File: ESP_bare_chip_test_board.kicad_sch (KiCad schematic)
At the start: 5 parts

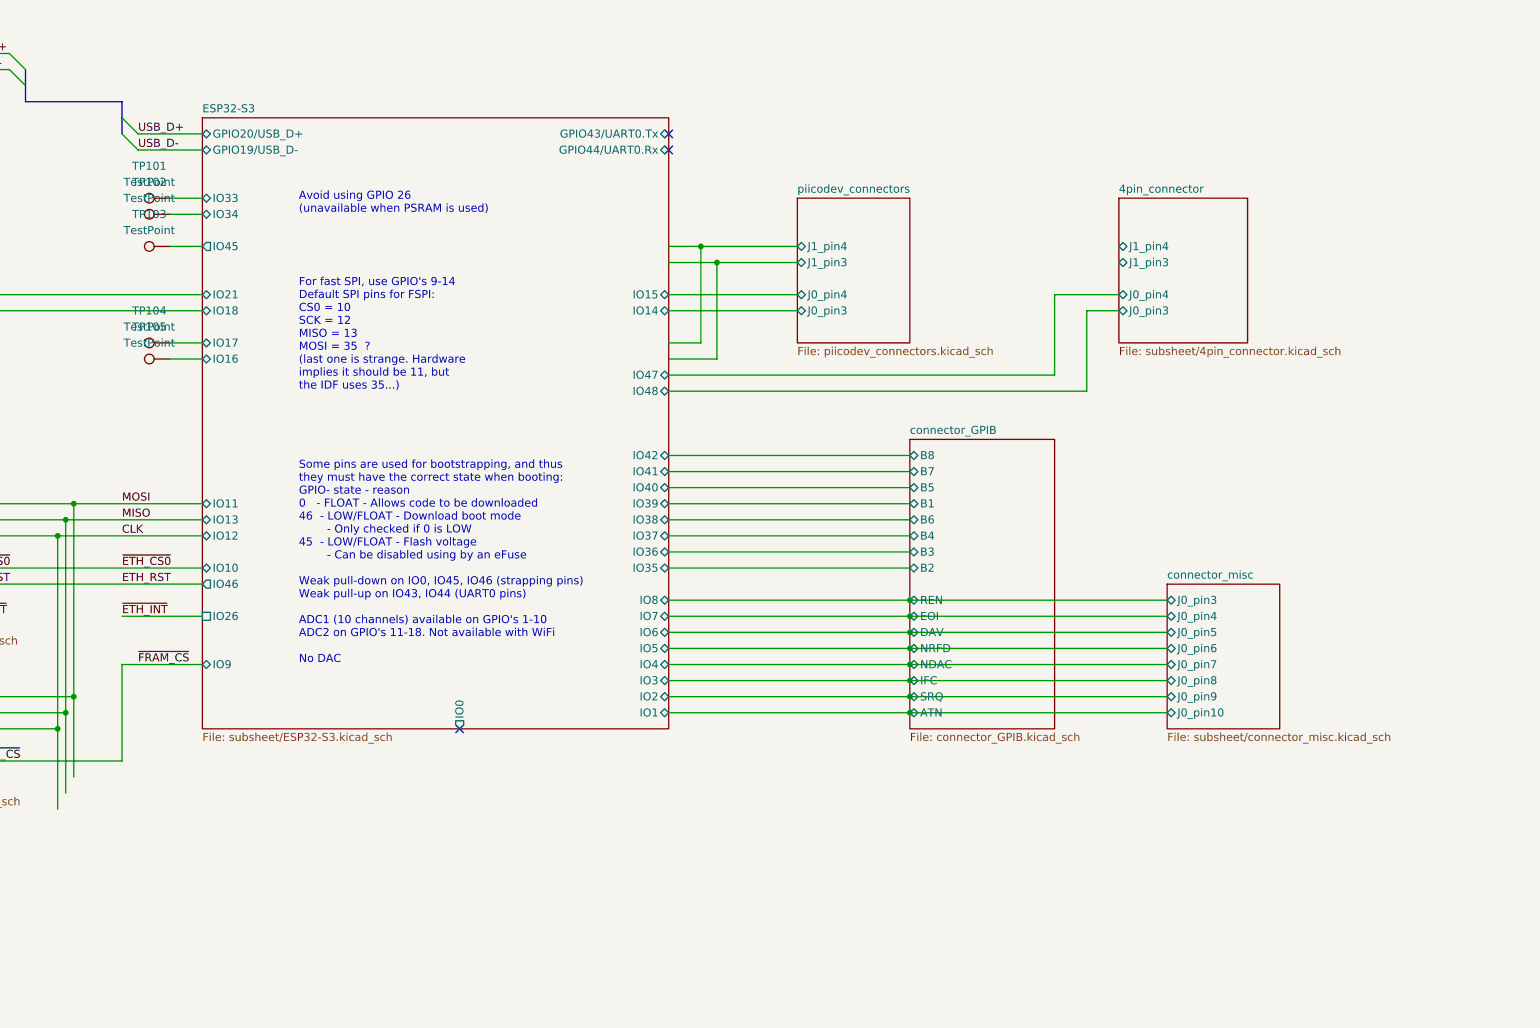
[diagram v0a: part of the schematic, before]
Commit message: Free up IO26 (to allow for PSRAM)
Had spare IO lines, so may as well use a different one to do ETH_INT
instead of IO26.
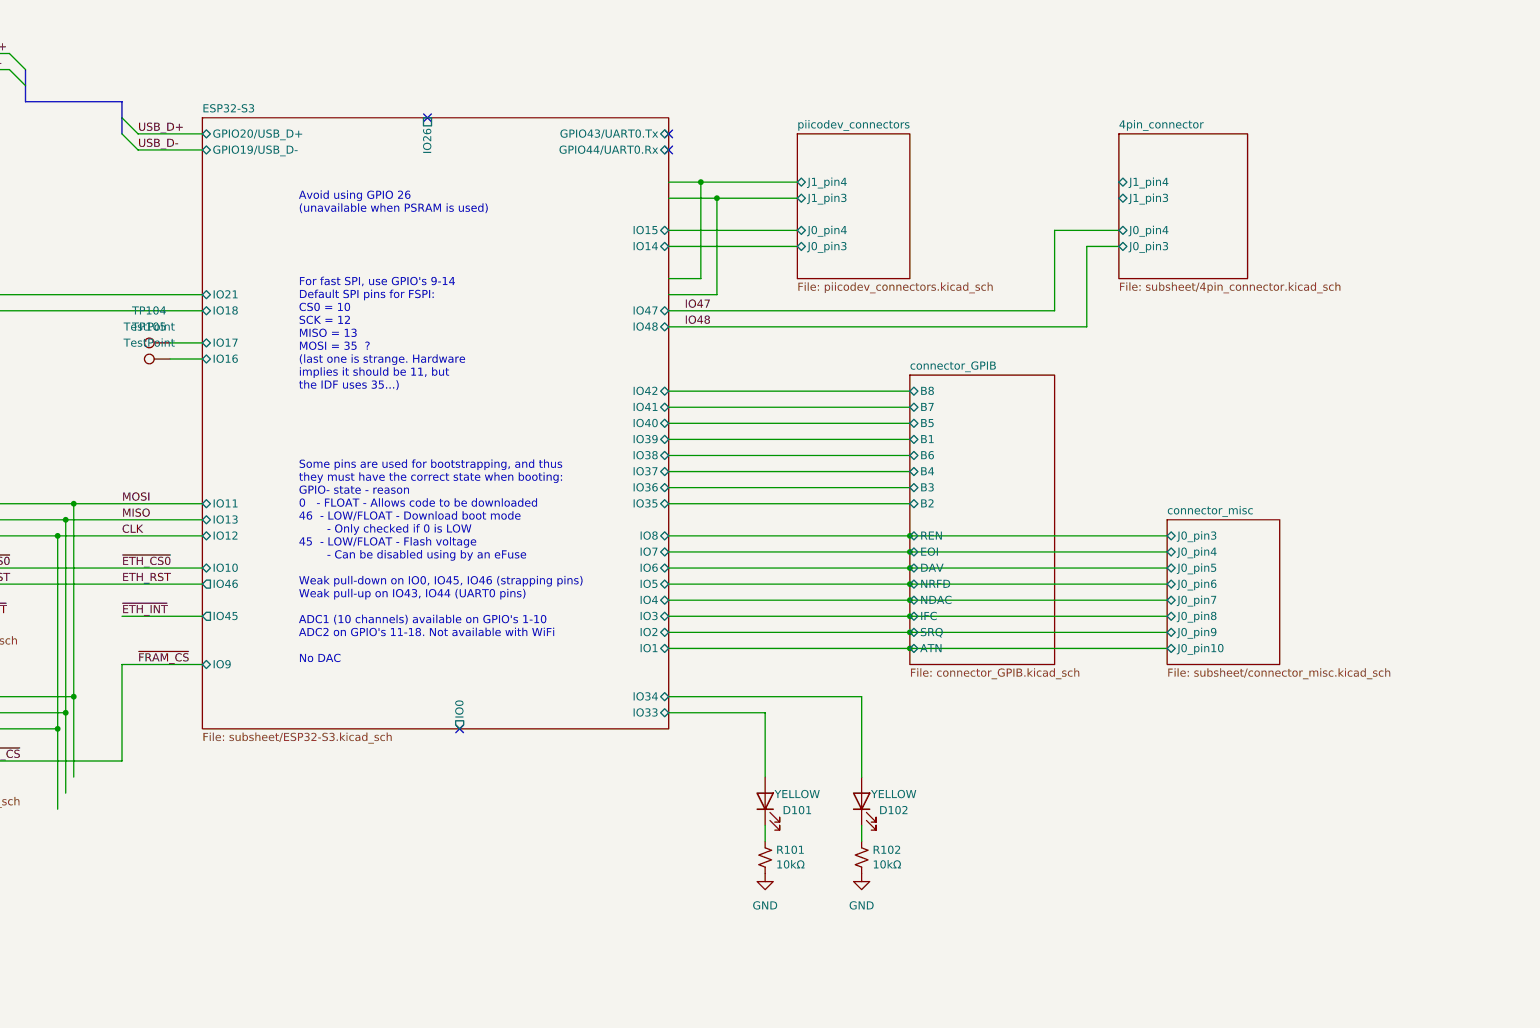
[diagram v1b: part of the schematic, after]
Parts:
- removed TP101, TP102, TP103: TestPoint, TestPoint:TestPoint_Pad_D2.0mm, symbol Connector:TestPoint
- added D101, D102: YELLOW, LED_SMD:LED_0603_1608Metric, symbol Device:LED
- added R101, R102: 10kΩ, Resistor_SMD:R_0603_1608Metric, symbol Device:R_Small_US
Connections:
- net ESP32-S3/IO33: now also D101.2 (A)
- net ESP32-S3/IO34: now also D102.2 (A)
- new net: D101.1 (K), R101.1
- new net: D102.1 (K), R102.1
- new net GND: R101.2, R102.2
- no-connect marks 3 -> 4

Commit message: Silkscreen work. Edit tittle block/version number
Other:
- company: (c) -> (c) Vincent Dalstra
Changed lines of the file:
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@@
 	(title_block
 		(title "Untitled 4-layer JLCPCB")
-		(date "1984/04/01")
-		(rev "v1.0.0")
-		(company "(c)")
-		(comment 1 "Drawn by:")
+		(date "2024-06-14")
+		(rev "1.0.0")
+		(company "(c) Vincent Dalstra")
+		(comment 1 "Drawn by: VGD")
 		(comment 2 "Check by:")
 	)

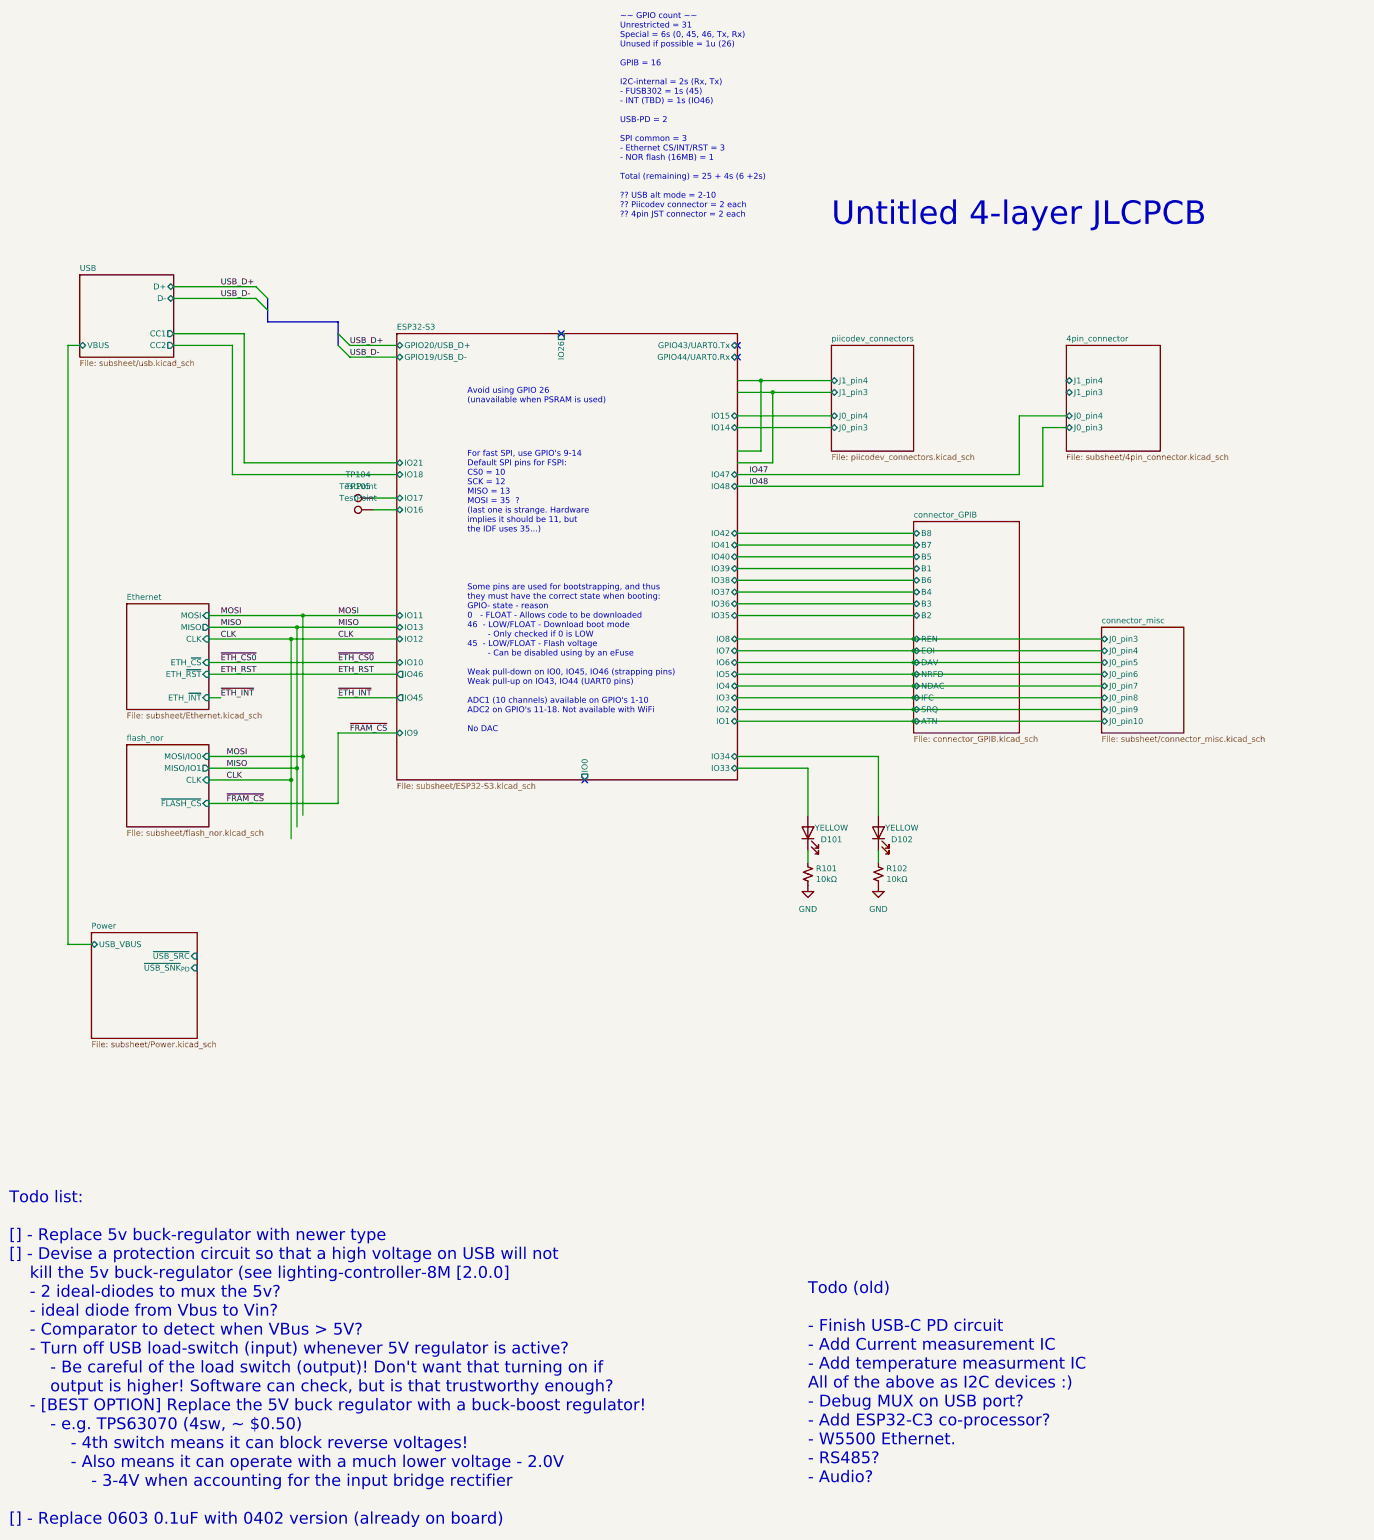
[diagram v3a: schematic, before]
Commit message: Move all subsheets into 'main' subsheet, below root
Keeping all the subsheets in a dedicated 'subsheet' folder makes things
much, much neater. However, specifying filepaths for subsheets has an
interesting problem; they use paths RELATIVE TO THE PARENT SHEET.

The consequence of is that if a subsheet is part of the root sheet, it
needs to be prefixed with 'subsheet/', but NOT if it's further down.
This inconsistency can be resolved by having a single 'main' sheet at
the top that doesn't move.

It's also useful to have a top-level space to put down changelogs,
descriptions etc.
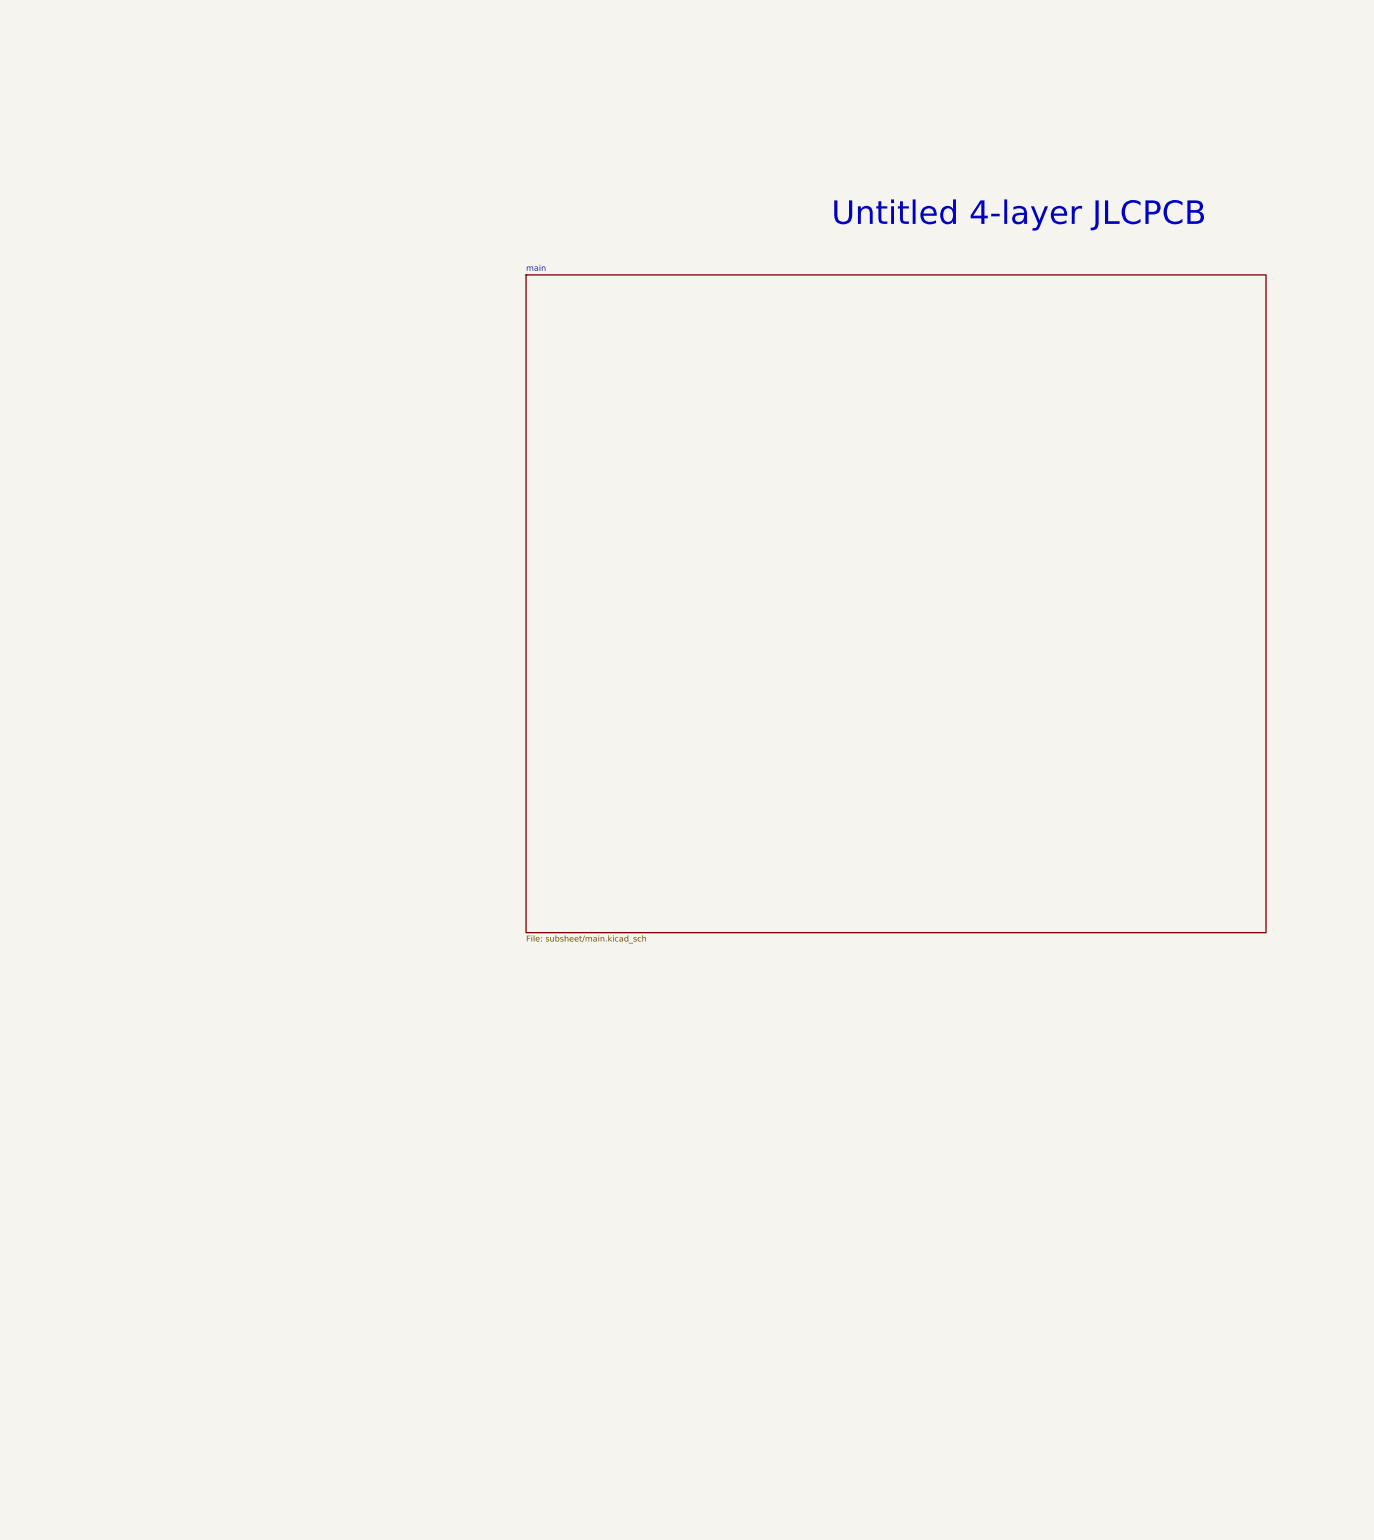
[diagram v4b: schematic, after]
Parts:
- removed D101, D102: YELLOW, LED_SMD:LED_0603_1608Metric, symbol Device:LED
- removed R101, R102: 10kΩ, Resistor_SMD:R_0603_1608Metric, symbol Device:R_Small_US
- removed TP104, TP105: TestPoint, TestPoint:TestPoint_Pad_D2.0mm, symbol Connector:TestPoint
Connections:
- no-connect marks 4 -> 0
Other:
- removed sheet 4pin_connector
- removed sheet ESP32-S3
- removed sheet Ethernet
- removed sheet Power
- removed sheet USB
- removed sheet connector_GPIB
- removed sheet connector_misc
- removed sheet flash_nor
- removed sheet piicodev_connectors
- added sheet main (subsheet/main.kicad_sch)
- note removed: "Avoid using GPIO 26 (unavailable when PSRAM is used)"
- note removed: "For fast SPI, use GPIO's 9-14 Default SPI pins for FSPI: CS0 = 10 SCK = 12 MISO = 13 MOSI = 35 ? (last one is strange. Hardware implies it should be 11, but the IDF uses 35...)"
- note removed: "Some pins are used for bootstrapping, and thus they must have the correct state when booting: GPIO- state - reason 0 - FLOAT - Allows code to be downloaded 46 - LOW/FLOAT - Download boot mode - Only checked if 0 is LOW 45 - LOW/FLOAT - Flash voltage - Can be disabled using by an eFuse Weak pull-down on IO0, IO45, IO46 (strapping pins) Weak pull-up on IO43, IO44 (UART0 pins) ADC1 (10 channels) ava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"
- note removed: "Todo (old) - Finish USB-C PD circuit - Add Current measurement IC - Add temperature measurment IC All of the above as I2C devices :) - Debug MUX on USB port? - Add ESP32-C3 co-processor? - W5500 Ethernet. - RS485? - Audio?"
- note removed: "Todo list: [] - Replace 5v buck-regulator with newer type [] - Devise a protection circuit so that a high voltage on USB will not kill the 5v buck-regulator (see lighting-controller-8M [2.0.0] - 2 ideal-diodes to mux the 5v? - ideal diode from Vbus to Vin? - Comparator to detect when VBus > 5V? - Turn off USB load-switch (input) whenever 5V regulator is active? - Be careful of the load switch (ou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"
- note removed: "~~ GPIO count ~~ Unrestricted = 31 Special = 6s (0, 45, 46, Tx, Rx) Unused if possible = 1u (26) GPIB = 16 I2C-internal = 2s (Rx, Tx) - FUSB302 = 1s (45) - INT (TBD) = 1s (IO46) USB-PD = 2 SPI common = 3 - Ethernet CS/INT/RST = 3 - NOR flash (16MB) = 1 Total (remaining) = 25 + 4s (6 +2s) ?? USB alt mode = 2-10 ?? Piicodev connector = 2 each ?? 4pin JST connector = 2 each"
